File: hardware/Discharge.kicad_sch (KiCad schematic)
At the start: 7 parts, among them Q2 CPH3351

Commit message: spaced out version
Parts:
- removed C8: 10nF, Capacitor_SMD:C_0603_1608Metric, symbol PUTM_EV_BMS_HV_Slave_2021-rescue:C_Small-Device
- removed R9: 100, Resistor_SMD:R_0603_1608Metric, symbol PUTM_EV_BMS_HV_Slave_2021-rescue:R_Small-Device
- added HS1: PAD, Connector_Wire:SolderWirePad_1x01_SMD_1x2mm, symbol Mechanical:Heatsink_Pad
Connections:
- new net THERMAL: HS1.1

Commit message: finished layout
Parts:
- removed HS1: PAD, Connector_Wire:SolderWirePad_1x01_SMD_1x2mm, symbol Mechanical:Heatsink_Pad
- added F1: 6V/6A, Samacsys:1206L075SLYR, symbol 1206l600slwr:1206L600SLWR
- D1: Manufacturer_Part_Number (none) -> 150060SS75000; Mouser Part Number (none) -> 710-150060SS75000; Mouser Price/Stock (none) -> https://www.mouser.pl/ProductDetail/Wurth-Elektronik/150060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
- Q2: Manufacturer_Part_Number (none) -> MMFTP3401; Mouser Part Number (none) -> 637-MMFTP3401; Mouser Price/Stock (none) -> https://www.mouser.pl/ProductDetail/Diotec-Semiconductor/MM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
- R11: footprint Resistor_SMD:R_2512_6332Metric -> Samacsys:RESC6331X80N; Manufacturer_Part_Number (none) -> CRM2512QFW-10R0ELF; Mouser Part Number (none) -> 652-CRM2512QFW-10R0E; Mouser Price/Stock (none) -> https://www.mouser.pl/ProductDetail/Bourns/CRM2512QFW-10R0E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
- R12: Manufacturer_Part_Number (none) -> RT0603FRE07330RL; Mouser Part Number (none) -> 603-RT0603FRE07330RL; Mouser Price/Stock (none) -> https://www.mouser.pl/ProductDetail/YAGEO/RT0603FRE07330RL?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
- R13: Manufacturer_Part_Number (none) -> RT0603FRE073K3L; Mouser Part Number (none) -> 603-RT0603FRE073K3L; Mouser Price/Stock (none) -> https://www.mouser.pl/ProductDetail/YAGEO/RT0603FRE073K3L?q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
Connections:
- net at R11.1, R12.1: now also F1.1; no longer Q2.3 (D)
- new net: F1.2, Q2.3 (D)
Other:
- note added: "thermaly bonded"
- moved on the sheet: D1, R11, R12

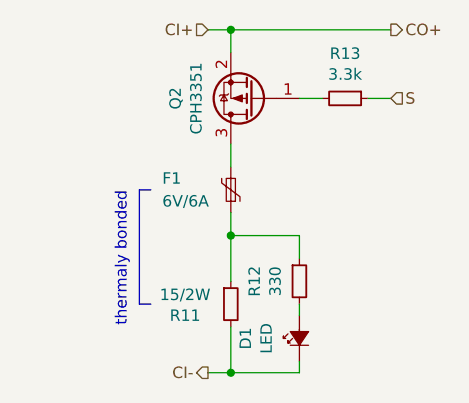
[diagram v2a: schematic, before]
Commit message: change from transformator to capacitive isolation between ltc, change ibias/icmp pin since they are incorrectly connected
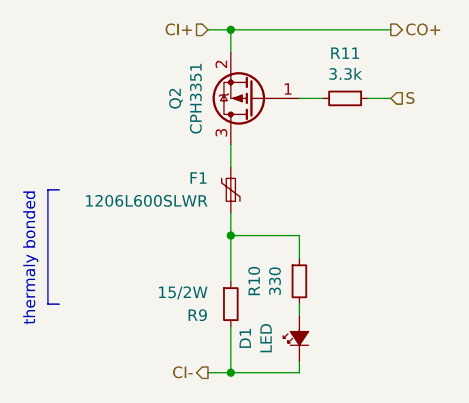
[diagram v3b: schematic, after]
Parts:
- F1: value 6V/6A -> 1206L600SLWR
- renumbered R12 to R10, R13 to R11, R11 to R9

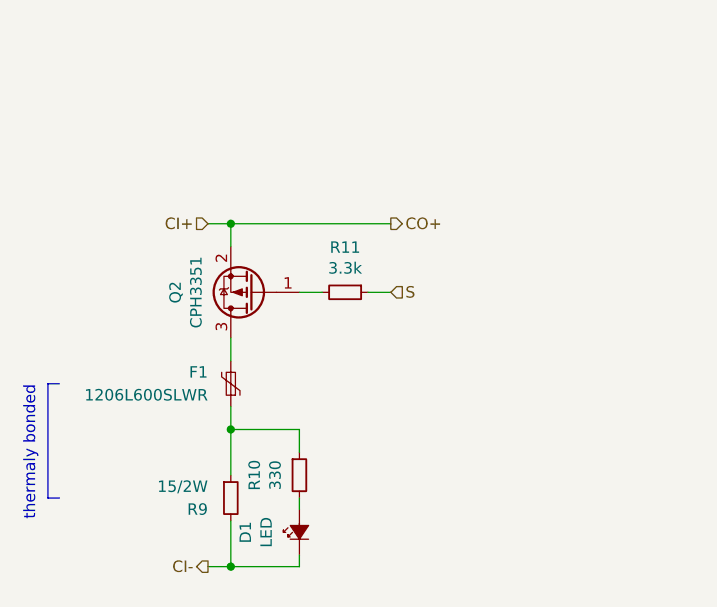
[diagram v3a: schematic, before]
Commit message: added temp disconnect, beautify schematic
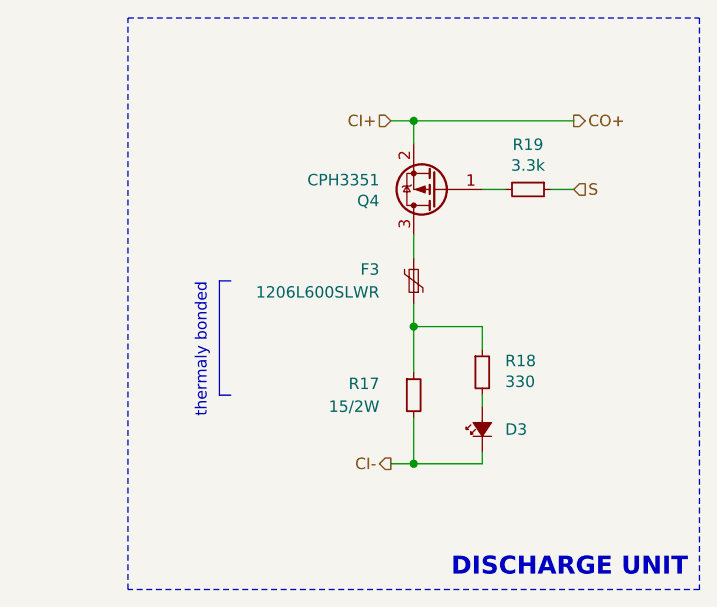
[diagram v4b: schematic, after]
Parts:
- renumbered D1 to D3, F1 to F3, Q2 to Q4, R9 to R17, R10 to R18, R11 to R19
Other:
- note added: "DISCHARGE UNIT"
- moved on the sheet: D3, F3, Q4, R17, R18, R19

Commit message: replaced signal transformer with rated capacitors, made the design more general for future use
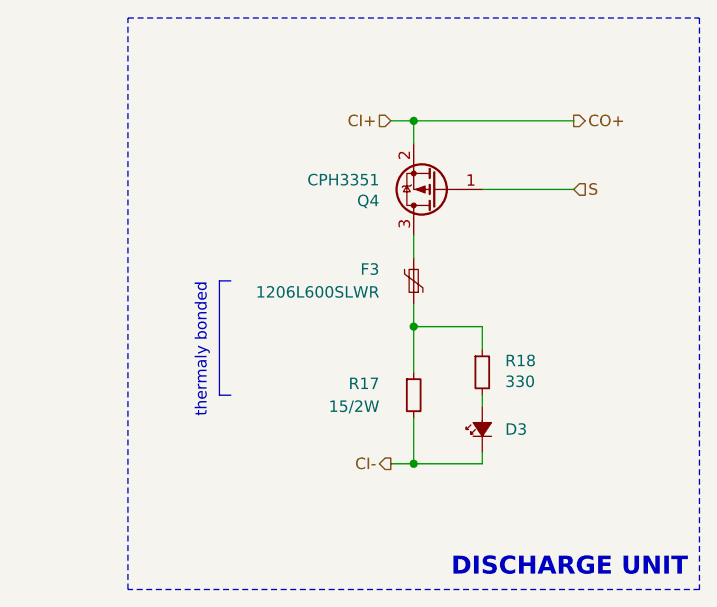
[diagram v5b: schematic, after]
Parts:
- removed R19: 3.3k, Resistor_SMD:R_0603_1608Metric, symbol PUTM_EV_BMS_HV_Slave_2021-rescue:R_Small-Device
- F3: footprint Samacsys:1206L075SLYR -> Fuse:Fuse_2512_6332Metric
- R17: footprint Samacsys:RESC6331X80N -> Resistor_SMD:R_2512_6332Metric
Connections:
- net S: now also Q4.1 (G)

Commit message: new schematic
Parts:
- removed F3: 1206L600SLWR, Fuse:Fuse_2512_6332Metric, symbol 1206l600slwr:1206L600SLWR
- removed Q4: CPH3351, Package_TO_SOT_SMD:SOT-23, symbol PUTM_EV_BMS_HV_Slave_2021-rescue:Q_PMOS_GSD-Device
- R17: value 15/2W -> 68/2W; CBOM HP2512-15R -> (none); Manufacturer_Part_Number CRM2512QFW-10R0ELF -> CR2512-JW-680ELF; Mouser Part Number 652-CRM2512QFW-10R0E -> 652-CR2512-JW-680ELF; Mouser Price/Stock https://www.mouser.pl/ProductDetail/Bourns/CRM2512QFW-10R0E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 -> https://www.mouser.pl/ProductDetail/Bourns/CR2512-JW-680ELF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
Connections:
- net CI- is gone; now on net S: D3.1 (K), R17.2
- net CI+: now also R17.1, R18.1
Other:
- note removed: "thermaly bonded"
- moved on the sheet: D3, R17, R18

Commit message: layout done
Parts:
- R17: value 68/2W -> 100/1W; footprint Resistor_SMD:R_2512_6332Metric -> Resistor_SMD:R_1210_3225Metric
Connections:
- net CI+ renamed C
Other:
- moved on the sheet: D3, R17, R18
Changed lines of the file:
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@@
 	(paper "A4")
 	(junction
-		(at 133.35 104.14)
+		(at 139.7 111.76)
 		(diameter 0)
 		(color 0 0 0 0)
 	)
 	(junction
-		(at 133.35 83.82)
+		(at 139.7 93.98)
 		(diameter 0)
 		(color 0 0 0 0)
 	)
-	(junction
-		(at 140.97 121.92)
-		(diameter 0)
-		(color 0 0 0 0)
-	)
-	(wire
-		(pts
-			(xy 133.35 83.82) (xy 151.13 83.82)
-		)
-		(stroke
-			(width 0)
-			(type default)
-		)
-	)
-	(wire
-		(pts
-			(xy 133.35 104.14) (xy 133.35 110.49)
-		)
-		(stroke
-			(width 0)
-			(type default)
-		)
-	)
-	(wire
-		(pts
-			(xy 140.97 121.92) (xy 151.13 121.92)
-		)
-		(stroke
-			(width 0)
-			(type default)
-		)
-	)
-	(wire
-		(pts
-			(xy 140.97 106.68) (xy 140.97 104.14)
-		)
-		(stroke
-			(width 0)
-			(type default)
-		)
-	)
-	(wire
-		(pts
-			(xy 133.35 104.14) (xy 140.97 104.14)
-		)
-		(stroke
-			(width 0)
-			(type default)
-		)
-	)
-	(wire
-		(pts
-			(xy 140.97 119.38) (xy 140.97 121.92)
-		)
-		(stroke
-			(width 0)
-			(type default)
-		)
-	)
-	(wire
-		(pts
-			(xy 130.81 83.82) (xy 133.35 83.82)
-		)
-		(stroke
-			(width 0)
-			(type default)
-		)
-	)
-	(wire
-		(pts
-			(xy 133.35 121.92) (xy 140.97 121.92)
-		)
-		(stroke
-			(width 0)
-			(type default)
-		)
-	)
-	(wire
-		(pts
-			(xy 133.35 115.57) (xy 133.35 121.92)
-		)
-		(stroke
-			(width 0)
-			(type default)
-		)
-	)
-	(wire
-		(pts
-			(xy 133.35 83.82) (xy 133.35 104.14)
-		)
-		(stroke
-			(width 0)
-			(type default)
-		)
-	)
-	(wire
-		(pts
-			(xy 140.97 111.76) (xy 140.97 114.3)
+	(wire
+		(pts
+			(xy 132.08 93.98) (xy 132.08 100.33)
+		)
+		(stroke
+			(width 0)
+			(type default)
+		)
+	)
+	(wire
+		(pts
+			(xy 139.7 111.76) (xy 149.86 111.76)
+		)
+		(stroke
+			(width 0)
+			(type default)
+		)
+	)
+	(wire
+		(pts
+			(xy 139.7 96.52) (xy 139.7 93.98)
+		)
+		(stroke
+			(width 0)
+			(type default)
+		)
+	)
+	(wire
+		(pts
+			(xy 132.08 93.98) (xy 139.7 93.98)
+		)
+		(stroke
+			(width 0)
+			(type default)
+		)
+	)
+	(wire
+		(pts
+			(xy 139.7 109.22) (xy 139.7 111.76)
+		)
+		(stroke
+			(width 0)
+			(type default)
+		)
+	)
+	(wire
+		(pts
+			(xy 139.7 93.98) (xy 149.86 93.98)
+		)
+		(stroke
+			(width 0)
+			(type default)
+		)
+	)
+	(wire
+		(pts
+			(xy 132.08 111.76) (xy 139.7 111.76)
+		)
+		(stroke
+			(width 0)
+			(type default)
+		)
+	)
+	(wire
+		(pts
+			(xy 132.08 105.41) (xy 132.08 111.76)
+		)
+		(stroke
+			(width 0)
+			(type default)
+		)
+	)
+	(wire
+		(pts
+			(xy 139.7 101.6) (xy 139.7 104.14)
 		)
 		(stroke
@@
 		)
 	)
-	(hierarchical_label "CO+"
-		(shape output)
-		(at 151.13 83.82 0)
+	(hierarchical_label "S"
+		(shape input)
+		(at 149.86 111.76 0)
 		(fields_autoplaced yes)
 		(effects
@@
 		)
 	)
-	(hierarchical_label "S"
+	(hierarchical_label "C"
 		(shape input)
-		(at 151.13 121.92 0)
+		(at 149.86 93.98 0)
 		(fields_autoplaced yes)
 		(effects
@@
 		)
 	)
-	(hierarchical_label "CI+"
-		(shape input)
-		(at 130.81 83.82 180)
-		(fields_autoplaced yes)
-		(effects
-			(font
-				(size 1.27 1.27)
-			)
-			(justify right)
-		)
-	)
 	(symbol
 		(lib_id "PUTM_EV_BMS_HV_Slave_2021-rescue:R_Small-Device")
-		(at 140.97 109.22 0)
+		(at 139.7 99.06 0)
 		(unit 1)
 		(exclude_from_sim no)
@@
 		(dnp no)
 		(property "Reference" "R18"
-			(at 143.51 107.95 0)
+			(at 142.24 97.79 0)
 			(effects
 				(font
@@
 		)
 		(property "Value" "330"
-			(at 143.51 110.2614 0)
+			(at 142.24 100.1014 0)
 			(effects
 				(font
@@
 		)
 		(property "Footprint" "Resistor_SMD:R_0603_1608Metric"
-			(at 140.97 109.22 0)
+			(at 139.7 99.06 0)
 			(effects
 				(font
@@
 		)
 		(property "Datasheet" "~"
-			(at 140.97 109.22 0)
+			(at 139.7 99.06 0)
 			(effects
 				(font
@@
 		)
 		(property "Description" ""
-			(at 140.97 109.22 0)
+			(at 139.7 99.06 0)
 			(effects
 				(font
@@
 		)
 		(property "Manufacturer_Part_Number" "RT0603FRE07330RL"
-			(at 140.97 109.22 0)
+			(at 139.7 99.06 0)
 			(effects
 				(font
@@
 		)
 		(property "Mouser Part Number" "603-RT0603FRE07330RL"
-			(at 140.97 109.22 0)
+			(at 139.7 99.06 0)
 			(effects
 				(font
@@
 		)
 		(property "Mouser Price/Stock" "https://www.mouser.pl/ProductDetail/YAGEO/RT0603FRE07330RL?qs=%2Ff7pOCXLR5eC%252B7ufUFQIvA%3D%3D"
-			(at 140.97 109.22 0)
+			(at 139.7 99.06 0)
 			(effects
 				(font
@@
 	(symbol
 		(lib_id "PUTM_EV_BMS_HV_Slave_2021-rescue:R_Small-Device")
-		(at 133.35 113.03 0)
+		(at 132.08 102.87 0)
 		(unit 1)
 		(exclude_from_sim no)
@@
 		(dnp no)
 		(property "Reference" "R17"
-			(at 129.54 111.76 0)
+			(at 128.27 101.6 0)
 			(effects
 				(font
@@
 			)
 		)
-		(property "Value" "68/2W"
-			(at 129.54 114.3 0)
+		(property "Value" "100/1W"
+			(at 128.27 104.14 0)
 			(effects
 				(font
@@
 			)
 		)
-		(property "Footprint" "Resistor_SMD:R_2512_6332Metric"
-			(at 133.35 113.03 0)
+		(property "Footprint" "Resistor_SMD:R_1210_3225Metric"
+			(at 132.08 102.87 0)
 			(effects
 				(font
@@
 		)
 		(property "Datasheet" "~"
-			(at 133.35 113.03 0)
+			(at 132.08 102.87 0)
 			(effects
 				(font
@@
 		)
 		(property "Description" ""
-			(at 133.35 113.03 0)
+			(at 132.08 102.87 0)
 			(effects
 				(font
@@
 		)
 		(property "CBOM" ""
-			(at 133.35 113.03 0)
+			(at 132.08 102.87 0)
 			(effects
 				(font
@@
 		)
 		(property "Manufacturer_Part_Number" "CR2512-JW-680ELF"
-			(at 133.35 113.03 0)
+			(at 132.08 102.87 0)
 			(effects
 				(font
@@
 		)
 		(property "Mouser Part Number" "652-CR2512-JW-680ELF"
-			(at 133.35 113.03 0)
+			(at 132.08 102.87 0)
 			(effects
 				(font
@@
 		)
 		(property "Mouser Price/Stock" "https://www.mouser.pl/ProductDetail/Bourns/CR2512-JW-680ELF?qs=sGAEpiMZZMvdGkrng054t3VembYjER8wDs7RjV0k1vk%3D"
-			(at 133.35 113.03 0)
+			(at 132.08 102.87 0)
 			(effects
 				(font
@@
 	(symbol
 		(lib_id "PUTM_EV_BMS_HV_Slave_2021-rescue:LED_Small_ALT-Device")
-		(at 140.97 116.84 90)
+		(at 139.7 106.68 90)
 		(unit 1)
 		(exclude_from_sim no)
@@
 		(dnp no)
 		(property "Reference" "D3"
-			(at 143.51 116.84 90)
+			(at 142.24 106.68 90)
 			(effects
 				(font
@@
 		)
 		(property "Value" "LED"
-			(at 137.3124 116.84 0)
+			(at 136.0424 106.68 0)
 			(effects
 				(font
@@
 		)
 		(property "Footprint" "LED_SMD:LED_0603_1608Metric"
-			(at 140.97 116.84 90)
+			(at 139.7 106.68 90)
 			(effects
 				(font
@@
 		)
 		(property "Datasheet" "~"
-			(at 140.97 116.84 90)
+			(at 139.7 106.68 90)
 			(effects
 				(font
@@
 		)
 		(property "Description" ""
-			(at 140.97 116.84 0)
+			(at 139.7 106.68 0)
 			(effects
 				(font
@@
 		)
 		(property "CBOM" "LL-S190SC-2S"
-			(at 140.97 116.84 0)
+			(at 139.7 106.68 0)
 			(effects
 				(font
@@
 		)
 		(property "Manufacturer_Name" ""
-			(at 140.97 116.84 0)
+			(at 139.7 106.68 0)
 			(effects
 				(font
@@
 		)
 		(property "Manufacturer_Part_Number" "150060SS75000"
-			(at 140.97 116.84 0)
+			(at 139.7 106.68 0)
 			(effects
 				(font
@@
 		)
 		(property "Mouser Part Number" "710-150060SS75000"
-			(at 140.97 116.84 0)
+			(at 139.7 106.68 0)
 			(effects
 				(font
@@
 		)
 		(property "Mouser Price/Stock" "https://www.mouser.pl/ProductDetail/Wurth-Elektronik/150060SS75000?qs=LlUlMxKIyB0oQaxwspeTEA%3D%3D"
-			(at 140.97 116.84 0)
-			(effects
-				(font
+			(at 139.7 106.68 0)
+			(effects
+				(font

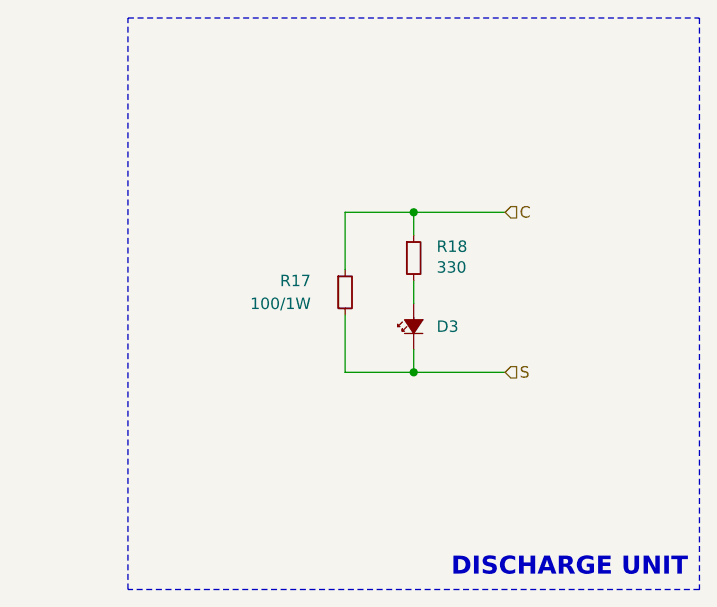
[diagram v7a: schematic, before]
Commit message: Bq ic balancing and measureing schematic part + main connector
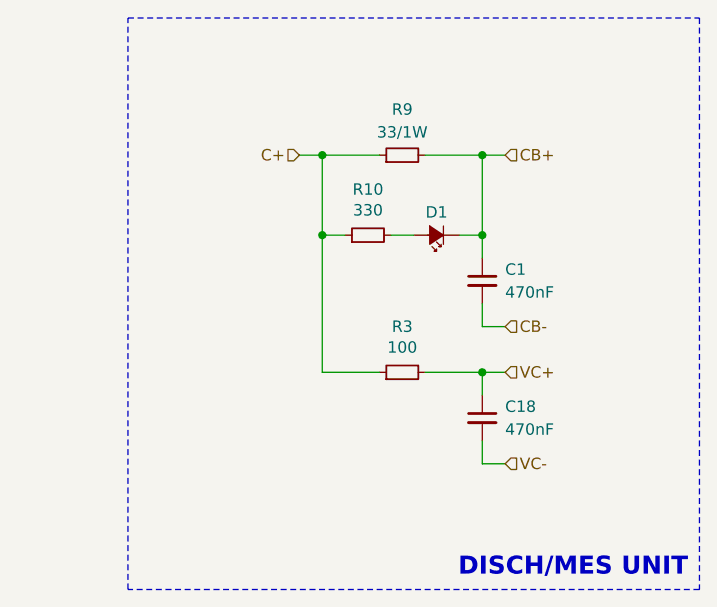
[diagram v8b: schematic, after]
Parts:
- added C1, C18: 470nF, Capacitor_SMD:C_0603_1608Metric, symbol Device:C_Small
- added R3: 100, Resistor_SMD:R_0603_1608Metric, symbol PUTM_EV_BMS_HV_Slave_2021-rescue:R_Small-Device
- R9: renamed from R17; value 100/1W -> 33/1W; footprint Resistor_SMD:R_1210_3225Metric -> Resistor_SMD:R_1206_3216Metric
- renumbered D3 to D1, R18 to R10
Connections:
- net C renamed C+
- net C+: now also R3.1
- net S renamed CB+
- net CB+: now also C1.1
- new net CB-: C1.2
- new net VC+: C18.1, R3.2
- new net VC-: C18.2
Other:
- note added: "DISCH/MES UNIT"
- note removed: "DISCHARGE UNIT"
- moved on the sheet: D1, R10, R9
